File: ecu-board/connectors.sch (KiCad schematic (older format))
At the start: 19 parts, among them J10 Injector connector, J11 MAP connector, J13 Chrankshaft Hall connector, J14 Camshaft Hall connector, J15 EGO connector, J2 Battery power conenctor, J3 Button input connector, J4 Motor conenctor, J5 Serial DB9 connector, J6 Ignition 1 connector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

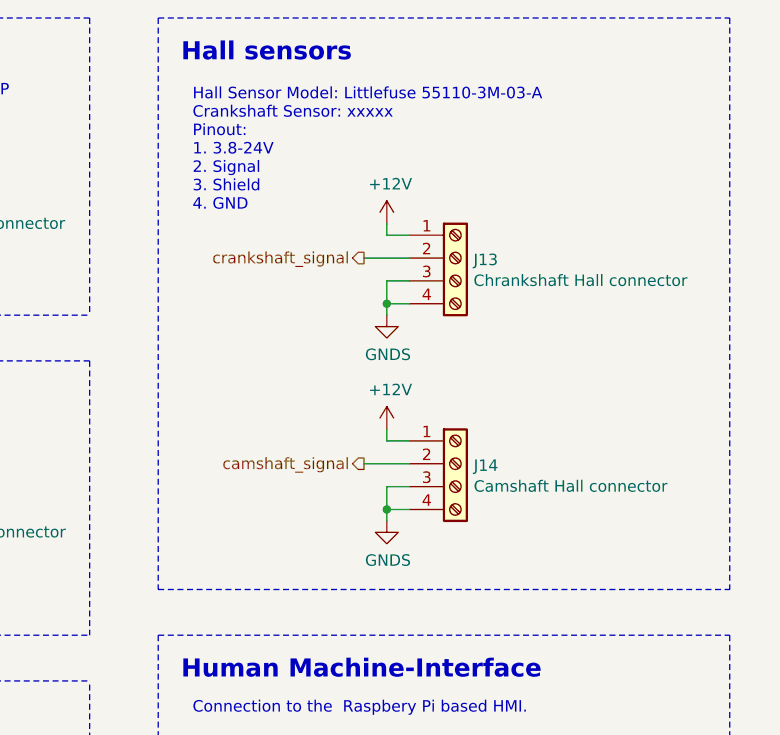
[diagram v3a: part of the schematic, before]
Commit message: Update crankshaft sensor model.
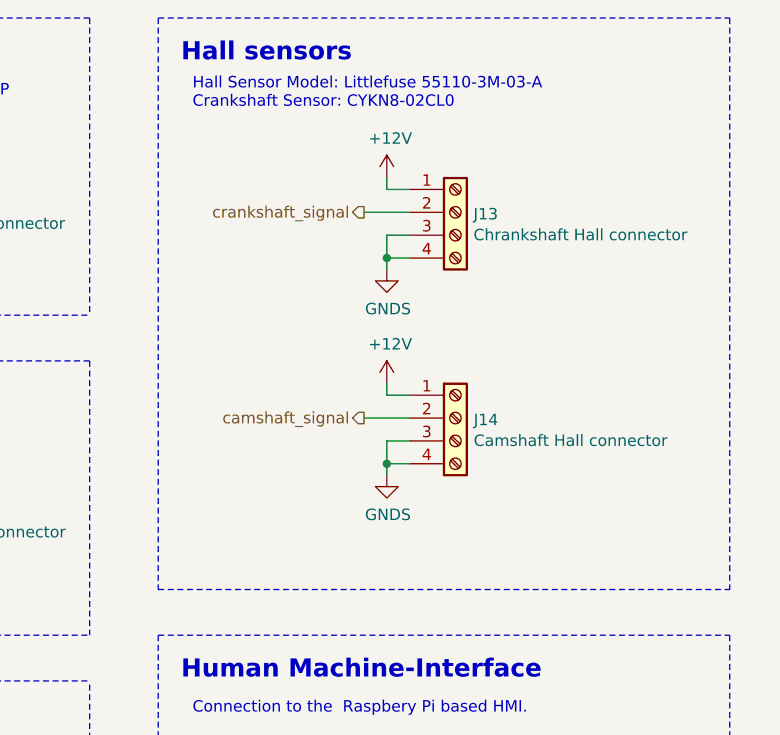
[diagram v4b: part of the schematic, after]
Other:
- note added: "Hall Sensor Model: Littlefuse 55110-3M-03-A\nCrankshaft Sensor: CYKN8-02CL0"
- note removed: "Hall Sensor Model: Littlefuse 55110-3M-03-A\nCrankshaft Sensor: xxxxx\nPinout:\n1. 3.8-24V\n2. Signal\n3. Shield\n4. GND"
- moved on the sheet: J13, J14
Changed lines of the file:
@@
 L power:+12V #PWR020
 U 1 1 5C5707AA
-P 9350 1800
-F 0 "#PWR020" H 9350 1650 50  0001 C CNN
-F 1 "+12V" H 9365 1973 50  0000 C CNN
-F 2 "" H 9350 1800 50  0001 C CNN
-F 3 "" H 9350 1800 50  0001 C CNN
-	1    9350 1800
-	1    0    0    -1
-$EndComp
-Wire Wire Line
-	9350 1800 9350 1850
-Wire Wire Line
-	9350 1850 9450 1850
+P 9350 1600
+F 0 "#PWR020" H 9350 1450 50  0001 C CNN
+F 1 "+12V" H 9365 1773 50  0000 C CNN
+F 2 "" H 9350 1600 50  0001 C CNN
+F 3 "" H 9350 1600 50  0001 C CNN
+	1    9350 1600
+	1    0    0    -1
+$EndComp
+Wire Wire Line
+	9350 1600 9350 1650
+Wire Wire Line
+	9350 1650 9450 1650
 $Comp
 L power:+12V #PWR022
 U 1 1 5C5707D6
-P 9350 2700
-F 0 "#PWR022" H 9350 2550 50  0001 C CNN
-F 1 "+12V" H 9365 2873 50  0000 C CNN
-F 2 "" H 9350 2700 50  0001 C CNN
-F 3 "" H 9350 2700 50  0001 C CNN
-	1    9350 2700
-	1    0    0    -1
-$EndComp
-Wire Wire Line
-	9350 2700 9350 2750
-Wire Wire Line
-	9350 2750 9450 2750
+P 9350 2500
+F 0 "#PWR022" H 9350 2350 50  0001 C CNN
+F 1 "+12V" H 9365 2673 50  0000 C CNN
+F 2 "" H 9350 2500 50  0001 C CNN
+F 3 "" H 9350 2500 50  0001 C CNN
+	1    9350 2500
+	1    0    0    -1
+$EndComp
+Wire Wire Line
+	9350 2500 9350 2550
+Wire Wire Line
+	9350 2550 9450 2550
 $Comp
 L power:GNDS #PWR021
 U 1 1 5C570990
-P 9350 2200
-F 0 "#PWR021" H 9350 1950 50  0001 C CNN
-F 1 "GNDS" H 9355 2027 50  0000 C CNN
-F 2 "" H 9350 2200 50  0001 C CNN
-F 3 "" H 9350 2200 50  0001 C CNN
-	1    9350 2200
-	1    0    0    -1
-$EndComp
-Wire Wire Line
-	9350 2200 9350 2150
-Wire Wire Line
-	9350 2150 9450 2150
+P 9350 2000
+F 0 "#PWR021" H 9350 1750 50  0001 C CNN
+F 1 "GNDS" H 9355 1827 50  0000 C CNN
+F 2 "" H 9350 2000 50  0001 C CNN
+F 3 "" H 9350 2000 50  0001 C CNN
+	1    9350 2000
+	1    0    0    -1
+$EndComp
+Wire Wire Line
+	9350 2000 9350 1950
+Wire Wire Line
+	9350 1950 9450 1950
 $Comp
 L power:GNDS #PWR023
 U 1 1 5C5709C2
-P 9350 3100
-F 0 "#PWR023" H 9350 2850 50  0001 C CNN
-F 1 "GNDS" H 9355 2927 50  0000 C CNN
-F 2 "" H 9350 3100 50  0001 C CNN
-F 3 "" H 9350 3100 50  0001 C CNN
-	1    9350 3100
-	1    0    0    -1
-$EndComp
-Wire Wire Line
-	9350 3100 9350 3050
-Wire Wire Line
-	9350 3050 9450 3050
-Wire Wire Line
-	9350 3050 9350 2950
-Wire Wire Line
-	9350 2950 9450 2950
-Connection ~ 9350 3050
-Wire Wire Line
-	9350 2150 9350 2050
-Wire Wire Line
-	9350 2050 9450 2050
-Connection ~ 9350 2150
-Text Notes 8500 1750 0    50   ~ 0
-Hall Sensor Model: Littlefuse 55110-3M-03-A\nCrankshaft Sensor: xxxxx\nPinout:\n1. 3.8-24V\n2. Signal\n3. Shield\n4. GND
+P 9350 2900
+F 0 "#PWR023" H 9350 2650 50  0001 C CNN
+F 1 "GNDS" H 9355 2727 50  0000 C CNN
+F 2 "" H 9350 2900 50  0001 C CNN
+F 3 "" H 9350 2900 50  0001 C CNN
+	1    9350 2900
+	1    0    0    -1
+$EndComp
+Wire Wire Line
+	9350 2900 9350 2850
+Wire Wire Line
+	9350 2850 9450 2850
+Wire Wire Line
+	9350 2850 9350 2750
+Wire Wire Line
+	9350 2750 9450 2750
+Connection ~ 9350 2850
+Wire Wire Line
+	9350 1950 9350 1850
+Wire Wire Line
+	9350 1850 9450 1850
+Connection ~ 9350 1950
+Text Notes 8500 1300 0    50   ~ 0
+Hall Sensor Model: Littlefuse 55110-3M-03-A\nCrankshaft Sensor: CYKN8-02CL0
 Text Notes 8450 1100 0    79   ~ 16
 Hall sensors\n
@@
 	6250 2200 8050 2200
 Wire Wire Line
-	9250 1950 9450 1950
-Wire Wire Line
-	9250 2850 9450 2850
-Text HLabel 9250 1950 0    50   Output ~ 0
+	9250 1750 9450 1750
+Wire Wire Line
+	9250 2650 9450 2650
+Text HLabel 9250 1750 0    50   Output ~ 0
 crankshaft_signal
-Text HLabel 9250 2850 0    50   Output ~ 0
+Text HLabel 9250 2650 0    50   Output ~ 0
 camshaft_signal
 Text HLabel 6900 1750 0    50   Output ~ 0
@@
 L Connector:Screw_Terminal_01x04 J13
 U 1 1 5C5953F1
-P 9650 1950
-F 0 "J13" H 9729 1942 50  0000 L CNN
-F 1 "Chrankshaft Hall connector" H 9729 1851 50  0000 L CNN
-F 2 "" H 9650 1950 50  0001 C CNN
-F 3 "~" H 9650 1950 50  0001 C CNN
-F 4 "2315043, 2315064" H 9650 1950 50  0001 C CNN "Farnell"
-	1    9650 1950
+P 9650 1750
+F 0 "J13" H 9729 1742 50  0000 L CNN
+F 1 "Chrankshaft Hall connector" H 9729 1651 50  0000 L CNN
+F 2 "" H 9650 1750 50  0001 C CNN
+F 3 "~" H 9650 1750 50  0001 C CNN
+F 4 "2315043, 2315064" H 9650 1750 50  0001 C CNN "Farnell"
+	1    9650 1750
 	1    0    0    -1
 $EndComp
@@
 L Connector:Screw_Terminal_01x04 J14
 U 1 1 5C596299
-P 9650 2850
-F 0 "J14" H 9730 2842 50  0000 L CNN
-F 1 "Camshaft Hall connector" H 9730 2751 50  0000 L CNN
-F 2 "" H 9650 2850 50  0001 C CNN
-F 3 "~" H 9650 2850 50  0001 C CNN
-F 4 "2315043, 2315064" H 9650 2850 50  0001 C CNN "Farnell"
-	1    9650 2850
-	1    0    0    -1
-$EndComp
+P 9650 2650
+F 0 "J14" H 9730 2642 50  0000 L CNN
+F 1 "Camshaft Hall connector" H 9730 2551 50  0000 L CNN
+F 2 "" H 9650 2650 50  0001 C CNN
+F 3 "~" H 9650 2650 50  0001 C CNN
+F 4 "2315043, 2315064" H 9650 2650 50  0001 C CNN "Farnell"
+	1    9650 2650
+	1    0    0    -1
+$EndComp
